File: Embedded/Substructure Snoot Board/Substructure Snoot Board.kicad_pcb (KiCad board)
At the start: 4 copper layers, 71 parts, among them J1 D0 FFC, J2 D1 FFC, J3 L0 JST, J4 L1 JST, J5 XT30, Q1 CSD17577Q5A, Q2 CSD17577Q5A, Q3 CSD17573Q5B, Q4 CSD17577Q5A, U1 D0 FFC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

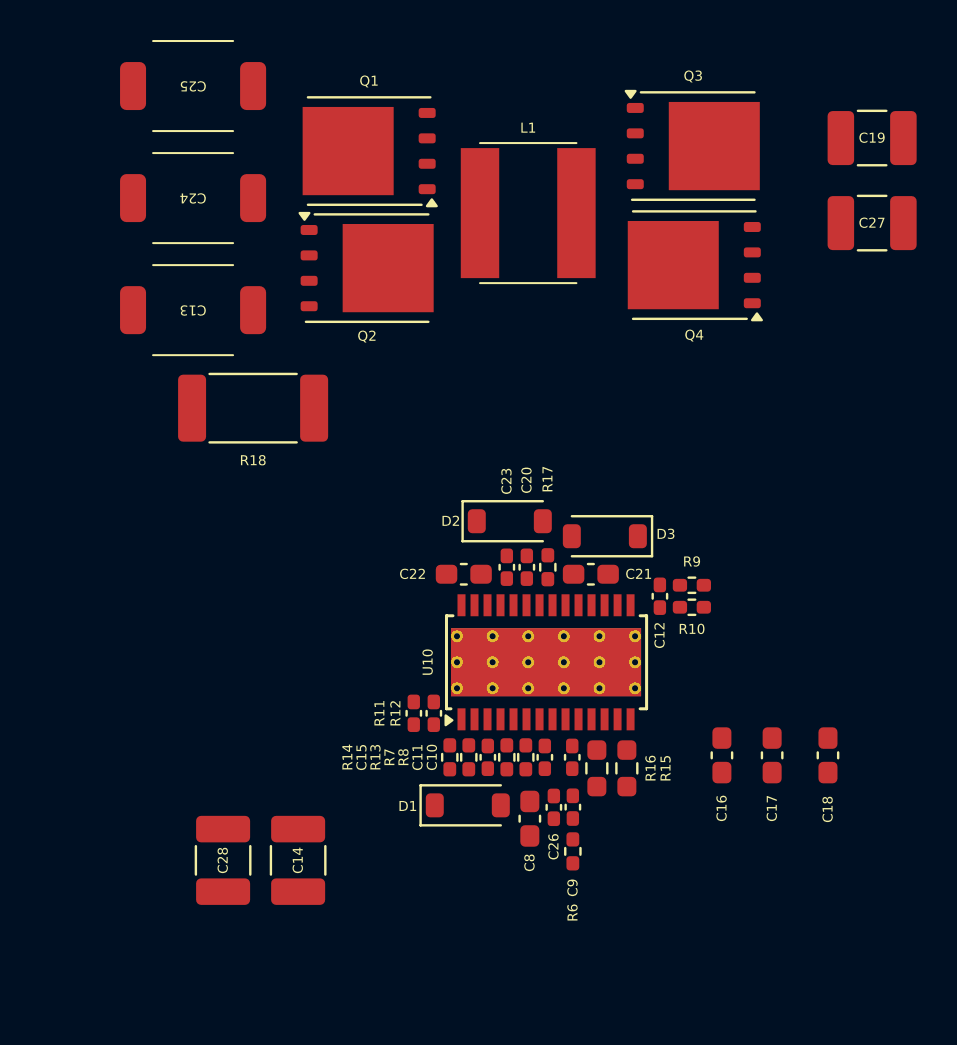
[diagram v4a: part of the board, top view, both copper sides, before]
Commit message: Added Buck Converter Power Component Space Optimisation
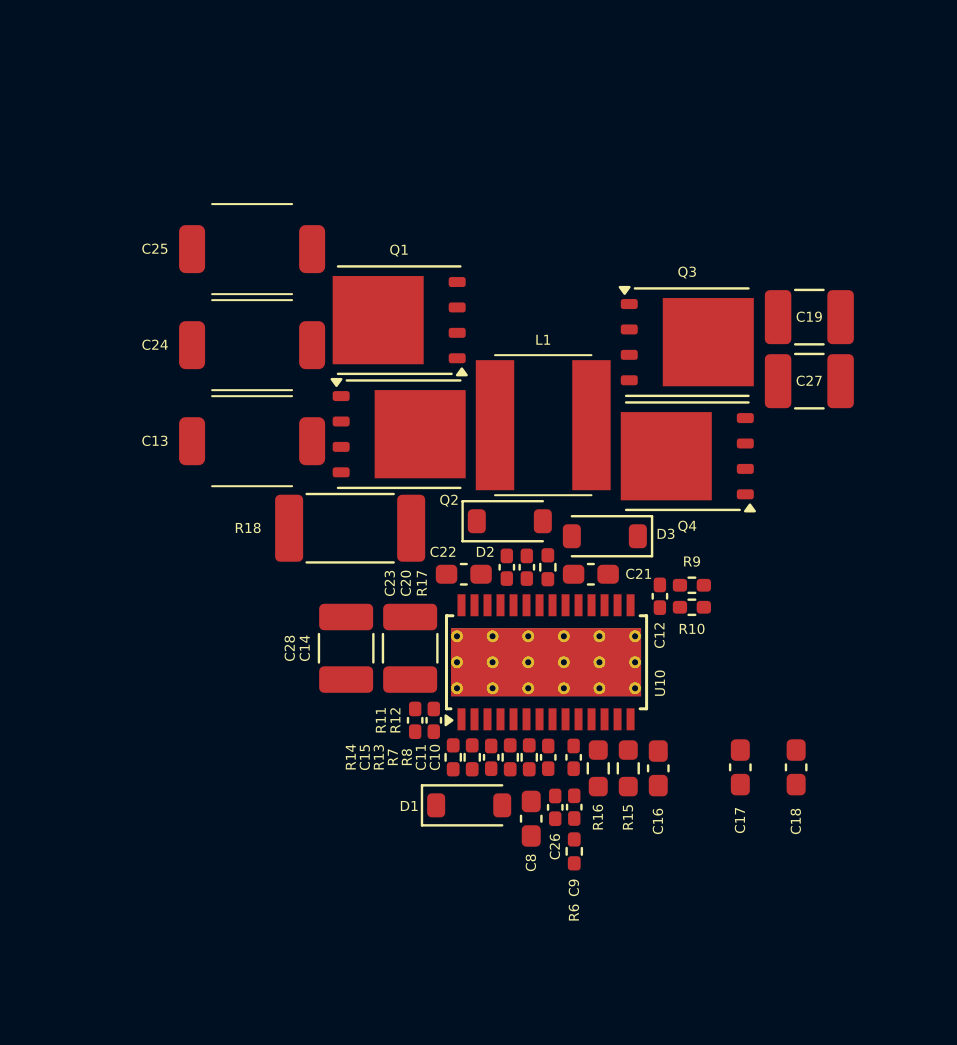
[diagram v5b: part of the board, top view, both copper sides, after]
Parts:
- moved C28 12.3 mm to (205.9, 94.2), turned to 90 degrees
- moved C14 12.0 mm to (209.1, 94.2), turned to 90 degrees
- moved L1 10.6 mm to (215.8, 83.1)
- moved Q3 9.80 mm to (222.9, 79.0)
- moved Q4 9.56 mm to (222.9, 84.7)
- moved C19 9.48 mm to (229.1, 77.7)
- moved C25 8.67 mm to (201.2, 74.3)
- moved Q1 8.58 mm to (208.6, 77.8)
- moved C27 8.50 mm to (229.1, 80.9)
- moved Q2 8.45 mm to (208.6, 83.5)
- moved C24 7.92 mm to (201.2, 79.1)
- moved R18 7.72 mm to (206.1, 88.2)
- moved C13 7.18 mm to (201.2, 83.9)
- moved C16 3.25 mm to (221.5, 100.2)
- moved C17 1.70 mm to (225.6, 100.2)
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
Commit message: Modified Component Placement for Implementation Ideation
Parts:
- C1, C13, C19, C2, C24, C25, C27, C3, D2, D3, ESP1, L1, Q1, Q2, Q3, Q4, R1, R18, U3, U4, U5: moved to B.Cu
- J5: footprint Connector_AMASS:AMASS_XT30U-M_1x02_P5.0mm_Vertical -> Connector_AMASS:AMASS_XT30PW-M_1x02_P2.50mm_Horizontal
- moved C19 168.5 mm to (60.7, 85.6), turned to 180 degrees
- moved C27 168.5 mm to (60.7, 88.8), turned to 180 degrees
- moved Q3 156.3 mm to (66.8, 86.8), turned to 180 degrees
- moved Q4 156.3 mm to (66.8, 92.5), turned to 0 degrees
- moved D3 148.1 mm to (70.9, 96.5), turned to 0 degrees
- moved L1 141.9 mm to (74.0, 90.0), turned to 180 degrees
- moved C10 141.5 mm to (76.3, 111.8)
- moved C11 141.5 mm to (75.0, 111.8)
- moved C12 141.5 mm to (80.6, 103.7)
- moved C14 141.5 mm to (68.1, 106.3)
- moved C15 141.5 mm to (71.2, 111.8)
- moved C16 141.5 mm to (80.5, 112.3)
- moved C17 141.5 mm to (84.6, 112.2)
- moved C18 141.5 mm to (87.4, 112.2)
- moved C20 141.5 mm to (73.9, 102.2)
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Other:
- board outline added: 60 x 80 mm

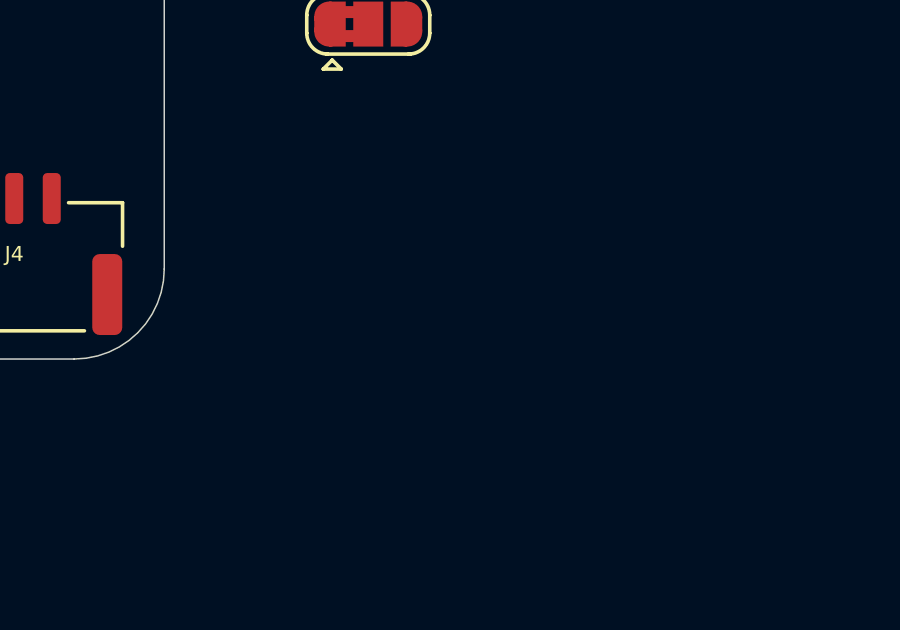
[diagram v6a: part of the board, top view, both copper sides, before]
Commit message: Added A JST (S JST Alternative Power Port) & S Pin Configs
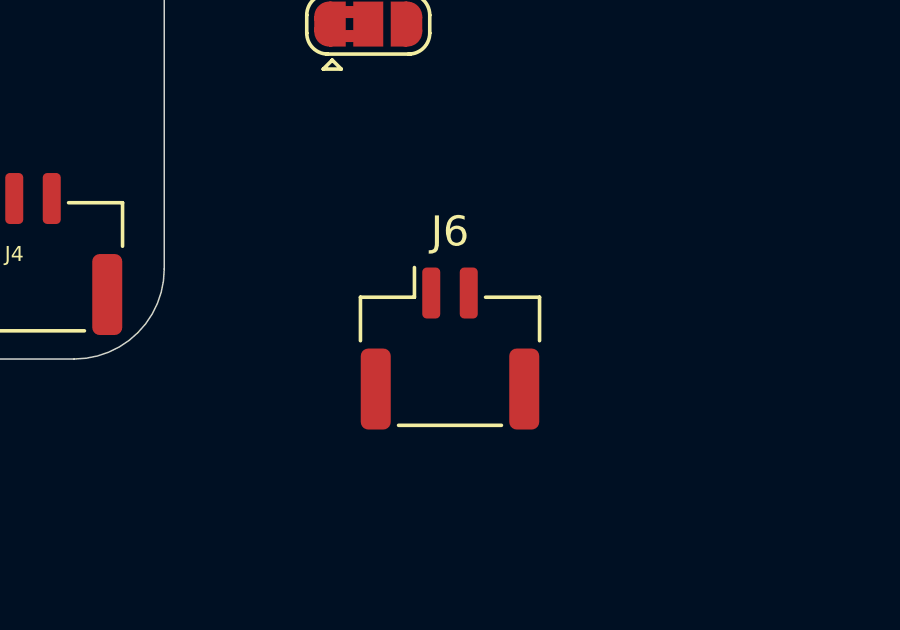
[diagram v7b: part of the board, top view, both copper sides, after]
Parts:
- added J6: A JST, Connector_JST:JST_GH_SM02B-GHS-TB_1x02-1MP_P1.25mm_Horizontal, F.Cu at (109.5, 74.7)
- J5: value XT30 -> S JST

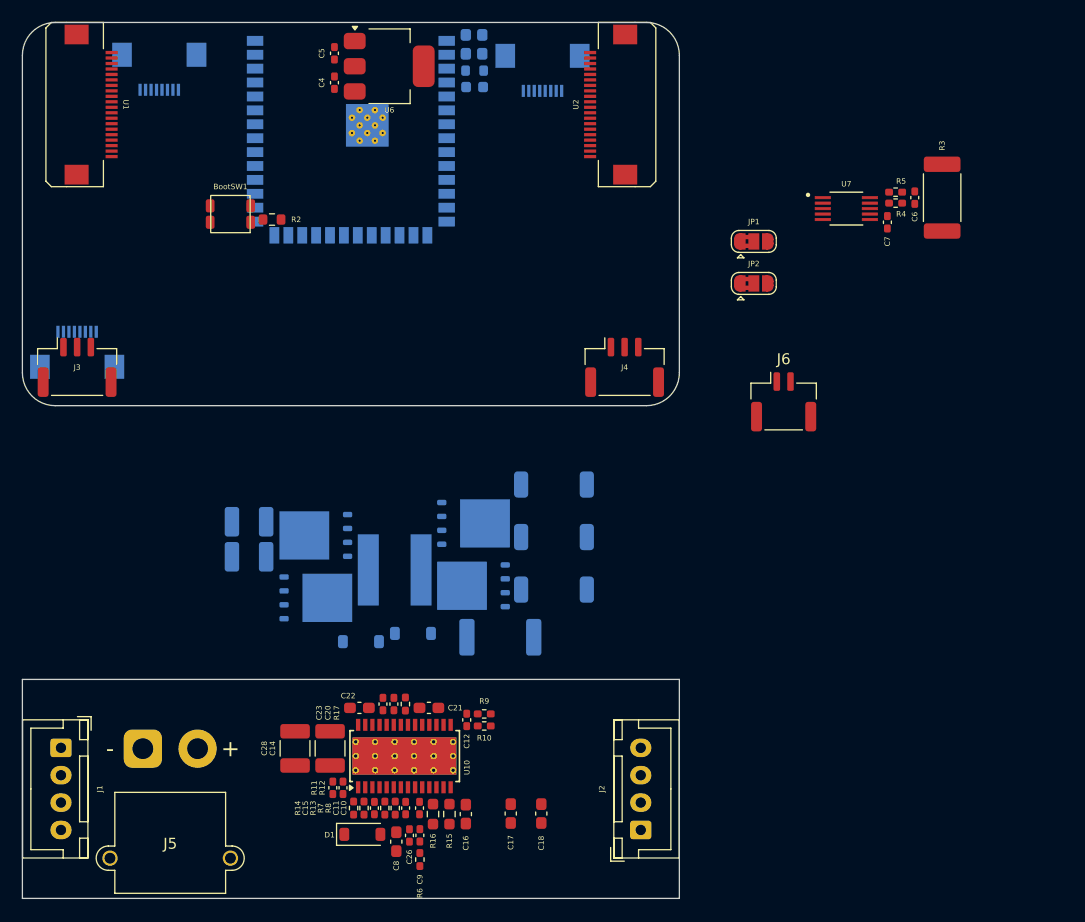
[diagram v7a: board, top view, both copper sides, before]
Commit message: Modified Component Placement for Board
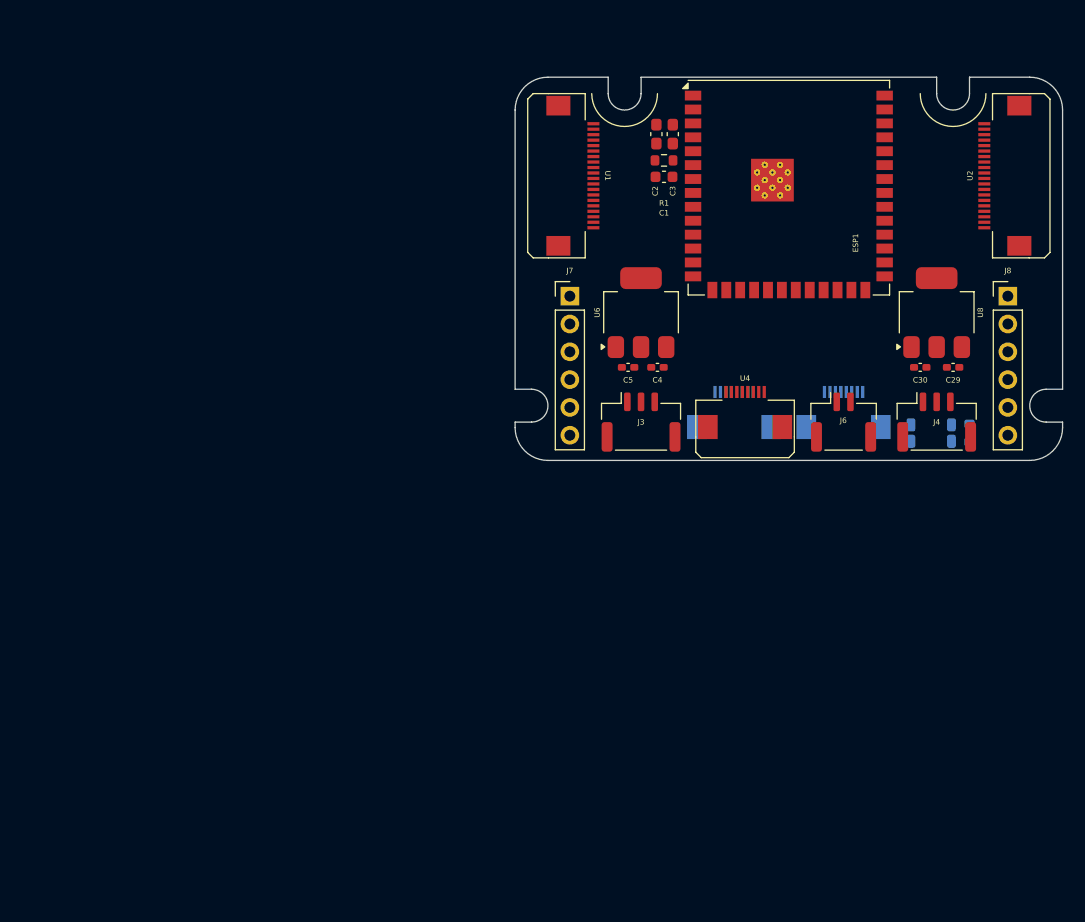
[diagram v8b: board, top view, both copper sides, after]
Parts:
- removed C10: 2nF 0ohm, Capacitor_SMD:C_0402_1005Metric_Pad0.74x0.62mm_HandSolder
- removed C11: 82pF 0ohm, Capacitor_SMD:C_0402_1005Metric_Pad0.74x0.62mm_HandSolder
- removed C12: 47pF 1mohms, Capacitor_SMD:C_0402_1005Metric_Pad0.74x0.62mm_HandSolder
- removed C13, C24, C25: 33uF 40mohm, Capacitors:EEFCX1E330R
- removed C14, C19, C27, C28: 47uF 3mohm, Capacitor_SMD:C_1210_3225Metric_Pad1.33x2.70mm_HandSolder
- removed C15: 100nF 39mohm, Resistor_SMD:R_0402_1005Metric_Pad0.72x0.64mm_HandSolder
- removed C16, C17, C18: 22uF 3.71mohm, Capacitor_SMD:C_0603_1608Metric_Pad1.08x0.95mm_HandSolder
- removed C20: 1uF 11.4mohm, Capacitor_SMD:C_0402_1005Metric_Pad0.74x0.62mm_HandSolder
- removed C21, C22: 100nF 50mohm, Capacitor_SMD:C_0603_1608Metric_Pad1.08x0.95mm_HandSolder
- removed C23: 100nF 1mohm, Capacitor_SMD:C_0402_1005Metric_Pad0.74x0.62mm_HandSolder
- removed C26, C9: 6.8nF 523mohm, Capacitor_SMD:C_0402_1005Metric_Pad0.74x0.62mm_HandSolder
- removed C6: 1uF, Capacitor_SMD:C_0402_1005Metric_Pad0.74x0.62mm_HandSolder
- removed C7: 0.1uF, Capacitor_SMD:C_0402_1005Metric_Pad0.74x0.62mm_HandSolder
- removed C8: 12nF 0ohm, Capacitor_SMD:C_0603_1608Metric_Pad1.08x0.95mm_HandSolder
- removed D1, D2, D3: 385mV 500mA, Diode_SMD:D_SOD-123
- removed J1: D0 FFC, Connector_JST:JST_XH_B4B-XH-A_1x04_P2.50mm_Vertical
- removed J2: D1 FFC, Connector_JST:JST_XH_B4B-XH-A_1x04_P2.50mm_Vertical
- removed J5: S JST, Connector_AMASS:AMASS_XT30PW-M_1x02_P2.50mm_Horizontal
- removed JP1, JP2: Bit Set, Jumper:SolderJumper-3_P1.3mm_Bridged2Bar12_RoundedPad1.0x1.5mm
- removed L1: 1uH 2.6mohm, Inductors:XAL7070-102ME
- removed Q1, Q2, Q4: CSD17577Q5A, Package_TO_SOT_SMD:TDSON-8-1
- removed Q3: CSD17573Q5B, Package_TO_SOT_SMD:TDSON-8-1
- removed R10, R9: 100, Resistor_SMD:R_0402_1005Metric_Pad0.72x0.64mm_HandSolder
- removed R11: 249K, Capacitor_SMD:C_0402_1005Metric_Pad0.74x0.62mm_HandSolder
- removed R12: 110K, Capacitor_SMD:C_0402_1005Metric_Pad0.74x0.62mm_HandSolder
- removed R13: 2K, Capacitor_SMD:C_0402_1005Metric_Pad0.74x0.62mm_HandSolder
- removed R14, R4, R5: 10, Resistor_SMD:R_0402_1005Metric_Pad0.72x0.64mm_HandSolder
- removed R15: 105K, Resistor_SMD:R_0603_1608Metric_Pad0.98x0.95mm_HandSolder
- removed R16: 20K, Resistor_SMD:R_0603_1608Metric_Pad0.98x0.95mm_HandSolder
- removed R17: 10K, Resistor_SMD:R_0402_1005Metric_Pad0.72x0.64mm_HandSolder
- removed R18: 5m, Resistor_SMD:R_2512_6332Metric_Pad1.40x3.35mm_HandSolder
- removed R3: Shunt CRF2512-FZ-R002ELF, Resistor_SMD:R_2512_6332Metric_Pad1.40x3.35mm_HandSolder
- removed R6: 732, Resistor_SMD:R_0402_1005Metric_Pad0.72x0.64mm_HandSolder
- removed R7: 93.1K, Resistor_SMD:R_0402_1005Metric_Pad0.72x0.64mm_HandSolder
- removed R8: 13K, Resistor_SMD:R_0402_1005Metric_Pad0.72x0.64mm_HandSolder
- removed U10: LM5176PWP, Package_SO:HTSSOP-28-1EP_4.4x9.7mm_P0.65mm_EP3.4x9.5mm_ThermalVias
- removed U7: INA220AIDGSR, INA220:SOP50P490X110-10N
- added C29: 0.1uf, Capacitor_SMD:C_0402_1005Metric_Pad0.74x0.62mm_HandSolder, F.Cu at (125.0, 71.5)
- added C30: 10uf, Capacitor_SMD:C_0402_1005Metric_Pad0.74x0.62mm_HandSolder, F.Cu at (122.0, 71.5)
- added J7: S Pins A, Connector_PinHeader_2.54mm:PinHeader_1x06_P2.54mm_Vertical, F.Cu at (90.0, 65.0)
- added J8: S Pins B, Connector_PinHeader_2.54mm:PinHeader_1x06_P2.54mm_Vertical, F.Cu at (130.0, 65.0)
- added U8: LD1117S50TR_SOT223, Package_TO_SOT_SMD:SOT-223-3_TabPin2, F.Cu at (123.5, 66.5)
- BootSW1, R2: moved to B.Cu
- C1, C2, C3, ESP1, R1, U4: moved to F.Cu
- moved U5 68.9 mm to (115.0, 74.4), turned to 180 degrees
- moved BootSW1 67.1 mm to (123.0, 77.5)
- moved R2 66.6 mm to (126.5, 77.5), turned to 90 degrees
- moved U4 61.2 mm to (106.0, 74.4), turned to 0 degrees
- moved J3 51.7 mm to (96.5, 76.5)
- moved U1 44.5 mm to (91.5, 54.0)
- moved ESP1 40.3 mm to (110.0, 55.1), turned to 0 degrees
- moved C4 39.3 mm to (98.0, 71.5), turned to 180 degrees
- moved C5 39.3 mm to (95.3, 71.5), turned to 180 degrees
- moved U2 36.6 mm to (128.5, 54.0)
- moved U3 33.7 mm to (105.0, 74.4), turned to 180 degrees
- moved U6 32.2 mm to (96.5, 66.5), turned to 90 degrees
- moved J4 28.9 mm to (123.5, 76.5)
- moved C3 20.6 mm to (99.4, 50.2)
- moved C1 19.1 mm to (98.6, 54.1), turned to 0 degrees
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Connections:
- C4 pad 1: +RAWVP -> +RAWVS
- U6 pad 3: +RAWVP -> +RAWVS
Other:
- board size 60 x 80 mm -> 50 x 35 mm
